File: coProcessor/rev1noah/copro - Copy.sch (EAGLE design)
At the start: 106 parts, among them IC1 STM32F405RGT6, J1 USB_MINI-B_SMT, J2 79107-08, J4 30320-6002HB, J5 5008730806

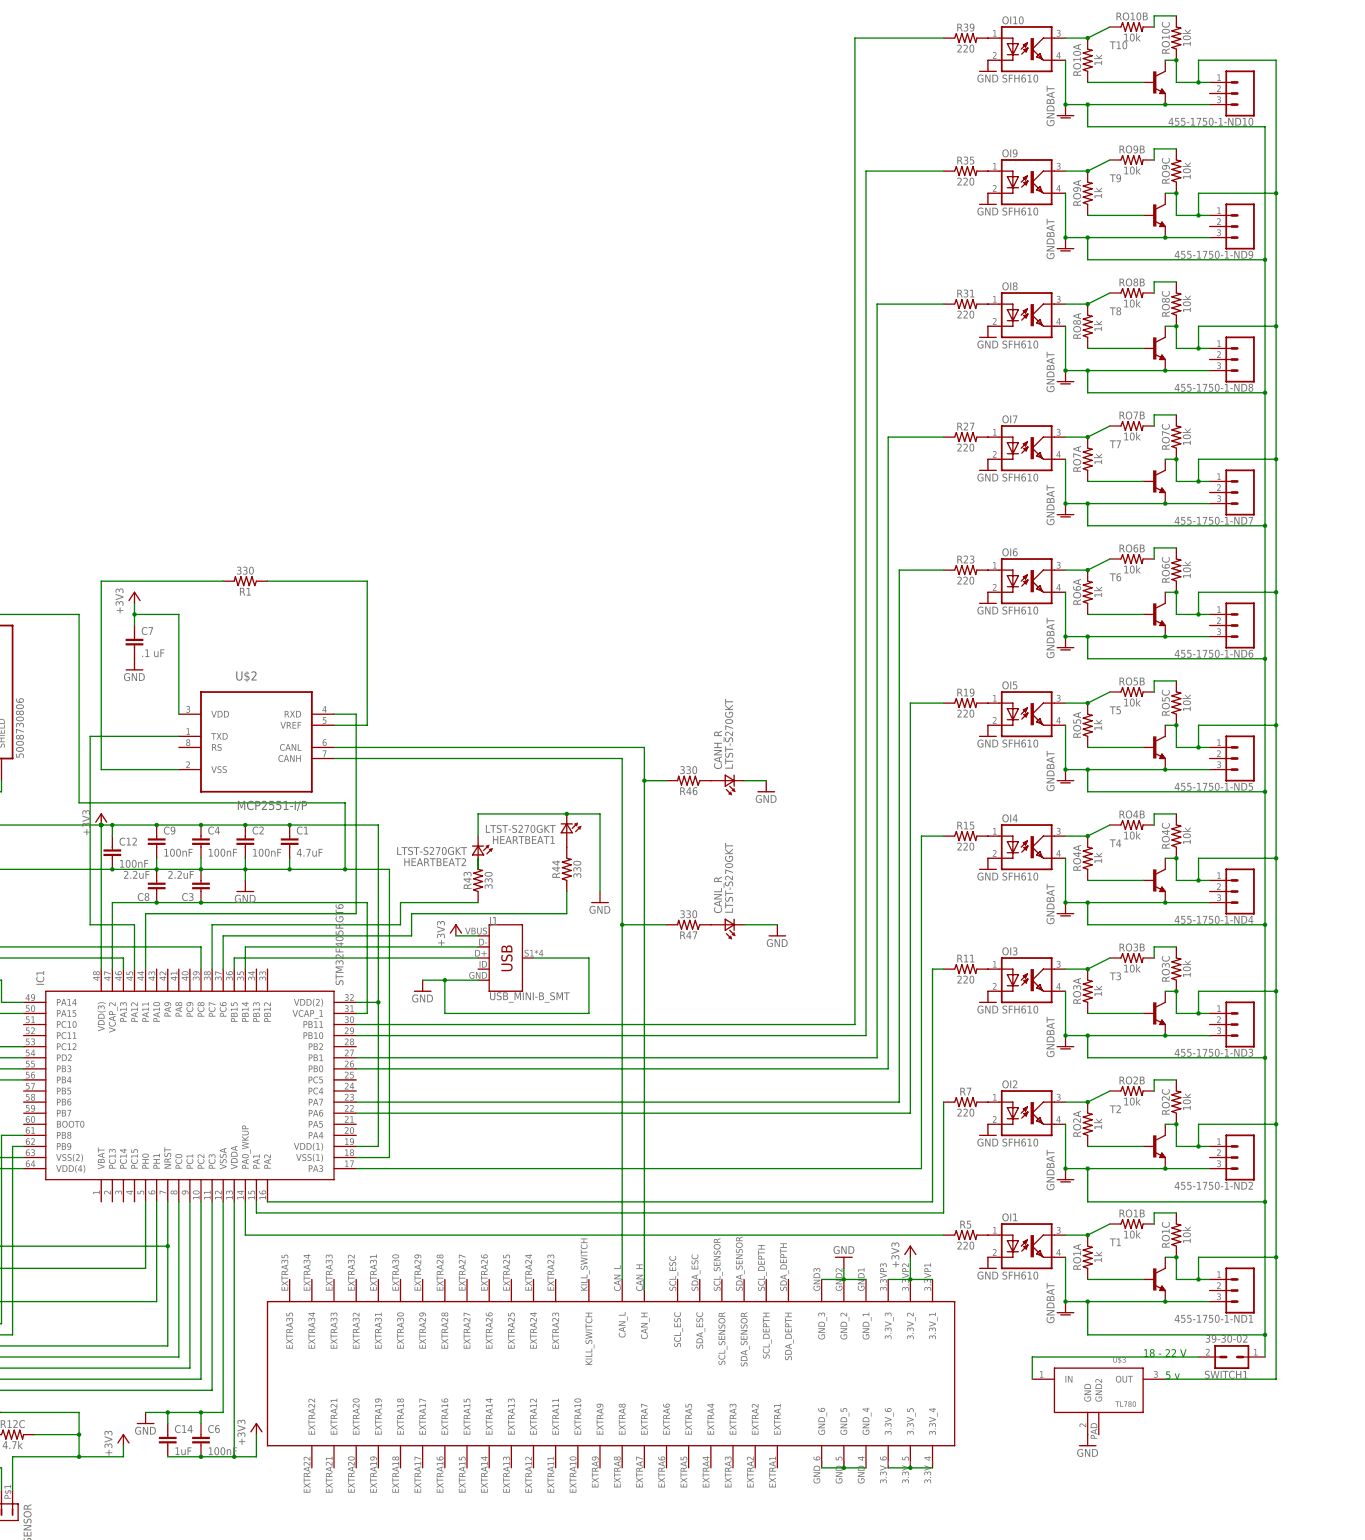
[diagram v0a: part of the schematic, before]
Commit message: The current official coprocessor board is now saved under the filename "copro - copy". I will change that. More importantly, the board is tentatively finished, atleast enough for others to check it, which i highly suggest.
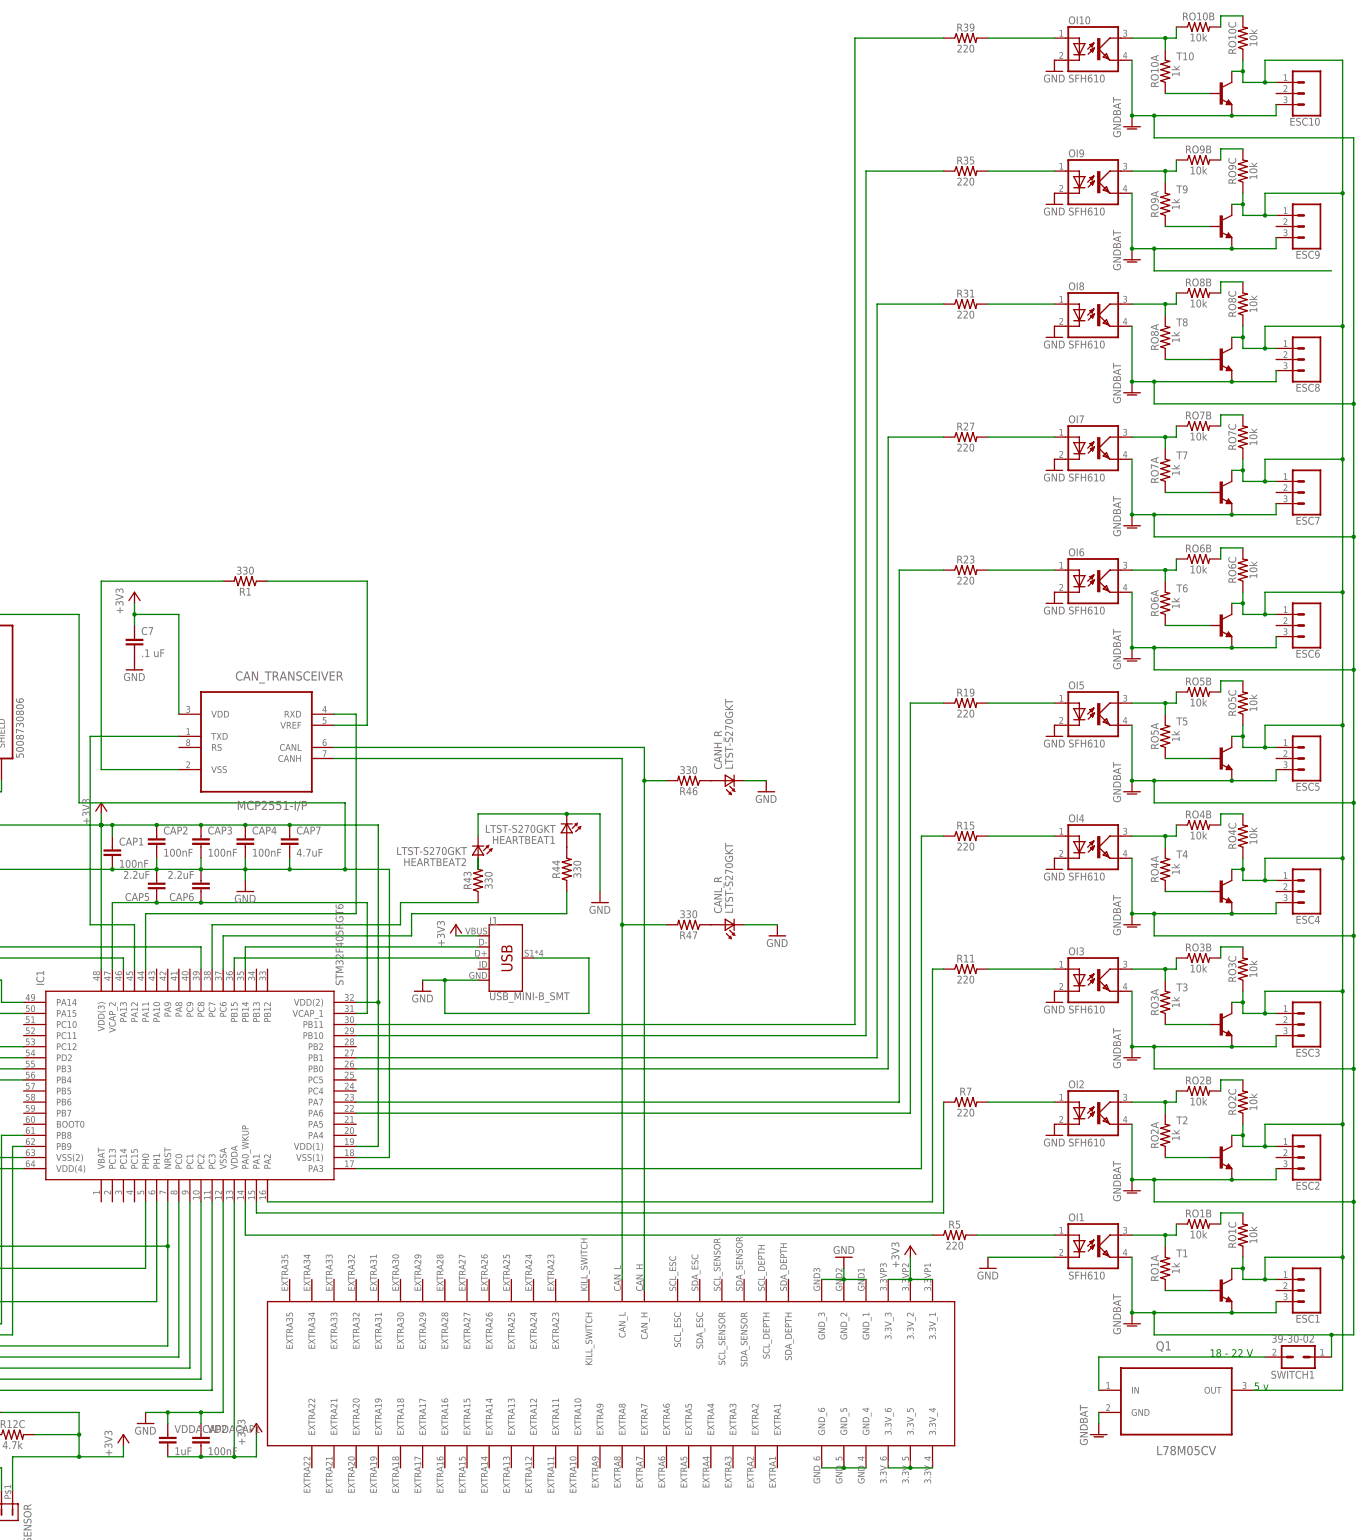
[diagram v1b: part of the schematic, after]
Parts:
- removed 455-1750-1-ND1, 455-1750-1-ND10, 455-1750-1-ND2, 455-1750-1-ND3, 455-1750-1-ND4, 455-1750-1-ND5, 455-1750-1-ND6, 455-1750-1-ND7, 455-1750-1-ND8, 455-1750-1-ND9: (no value), SparkFun-Connectors:CONN_03
- removed U$3: TL780_VREG, TL780_VREG:TL780_VREG
- added ESC1, ESC10, ESC2, ESC3, ESC4, ESC5, ESC6, ESC7, ESC8, ESC9: (no value), SparkFun-Connectors:CONN_03
- added Q1: L78M05CV, L78M05CV:L78M05CV
- renumbered C1 to CAP7, C12 to CAP1, C14 to VDDACAP2, C2 to CAP4, C3 to CAP6, C4 to CAP3, C6 to VDDACAP1, C8 to CAP5, C9 to CAP2, U$2 to CAN_TRANSCEIVER
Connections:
- net N$1 renamed POWER2O2
- net N$10 renamed POWER1O1
- net N$11 renamed PWM2
- net N$13 renamed OI1
- net N$15 renamed POWER1O2
- net N$16 renamed POWER2O3
- net N$17 renamed T3
- net N$19 renamed PWM3
- net N$2 renamed T1
- net N$22 renamed POWER1O3
- net N$23 renamed POWER2O4
- net N$24 renamed T4
- net N$26 renamed PWM4
- net N$29 renamed POWER1O4
- net N$3 renamed VCAP_2TO1
- net N$30 renamed POWER2O5
- net N$31 renamed T5
- net N$33 renamed PWM5
- net N$36 renamed POWER1O5
- net N$37 renamed POWER2O6
- net N$38 renamed T6
- net N$4 renamed PWM1
- net N$40 renamed PWM6
- net N$43 renamed POWER1O6
- net N$44 renamed POWER207
- net N$45 renamed T7
- net N$47 renamed PWM7
- net N$50 renamed POWER1O7
- net N$51 renamed POWER208
- net N$52 renamed T8
- net N$54 renamed PWM8
- net N$57 renamed POWER1O8
- net N$58 renamed POWER2O9
- net N$59 renamed T9
- net N$6 renamed POWER2O1
- net N$61 renamed PWM9
- net N$64 renamed POWER1O9
- net N$65 renamed POWER2O10
- net N$66 renamed T10
- net N$68 renamed PWM10
- net N$71 renamed POWER1O10
- net N$9 renamed T2
- net OPTO2 renamed OSC2
- removed net +3V3: C7.1, CAN_TRANSCEIVER.VDD, CAP1.1, CAP2.1, CAP3.1, CAP4.1, CAP7.1, DEPTH_SENSOR.1, IC1.VDD(1), IC1.VDD(2), IC1.VDD(3), IC1.VDD(4), IC1.VDDA, J1.VBUS, J2.1, J2.3, J2.5, J2.7, J4.1, J4.2, J5.VCC, POWERJACK.1, R12C.2, RI2C.2, VDDACAP1.2, VDDACAP2.2
- removed net N$18: 455-1750-1-ND1.1, 455-1750-1-ND10.1, 455-1750-1-ND2.1, 455-1750-1-ND3.1, 455-1750-1-ND4.1, 455-1750-1-ND5.1, 455-1750-1-ND6.1, 455-1750-1-ND7.1, 455-1750-1-ND8.1, 455-1750-1-ND9.1, RO10C.1, RO1C.1, RO2C.1, RO3C.1, RO4C.1, RO5C.1, RO6C.1, RO7C.1, RO8C.1, RO9C.1, T1.C, T10.C, T2.C, T3.C, T4.C, T5.C, T6.C, T7.C, T8.C, T9.C, U$3.OUT
- removed net N$7: SWITCH1.2, U$3.IN
- new net 18_22V: Q1.IN, SWITCH1.2
- new net 5V: ESC1.1, ESC10.1, ESC2.1, ESC3.1, ESC4.1, ESC5.1, ESC6.1, ESC7.1, ESC8.1, ESC9.1, Q1.OUT, RO10C.1, RO1C.1, RO2C.1, RO3C.1, RO4C.1, RO5C.1, RO6C.1, RO7C.1, RO8C.1, RO9C.1, T1.C, T10.C, T2.C, T3.C, T4.C, T5.C, T6.C, T7.C, T8.C, T9.C
- net 3.3V: now also C7.1, CAN_TRANSCEIVER.VDD, CAP1.1, CAP2.1, CAP3.1, CAP4.1, CAP7.1, DEPTH_SENSOR.1, IC1.VDD(1), IC1.VDD(2), IC1.VDD(3), IC1.VDD(4), IC1.VDDA, J1.VBUS, J2.1, J2.3, J2.5, J2.7, J4.1, J4.2, J5.VCC, POWERJACK.1, R12C.2, RI2C.2, VDDACAP1.2, VDDACAP2.2
- net GND: no longer U$3.GND
- net GNDBAT: now also ESC1.3, ESC10.3, ESC2.3, ESC3.3, ESC4.3, ESC5.3, ESC6.3, ESC7.3, ESC8.3, ESC9.3, Q1.GND; no longer 455-1750-1-ND1.3, 455-1750-1-ND10.3, 455-1750-1-ND2.3, 455-1750-1-ND3.3, 455-1750-1-ND4.3, 455-1750-1-ND5.3, 455-1750-1-ND6.3, 455-1750-1-ND7.3, 455-1750-1-ND8.3, 455-1750-1-ND9.3
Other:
- moved on the sheet: OI1, OI10, OI2, OI3, OI4, OI5, OI6, OI7, OI8, OI9, R5, RO10A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
